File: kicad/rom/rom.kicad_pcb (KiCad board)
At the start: 2 copper layers, 102.5 x 30 mm, 4 parts, among them J1 Board Connector, U1 28C256

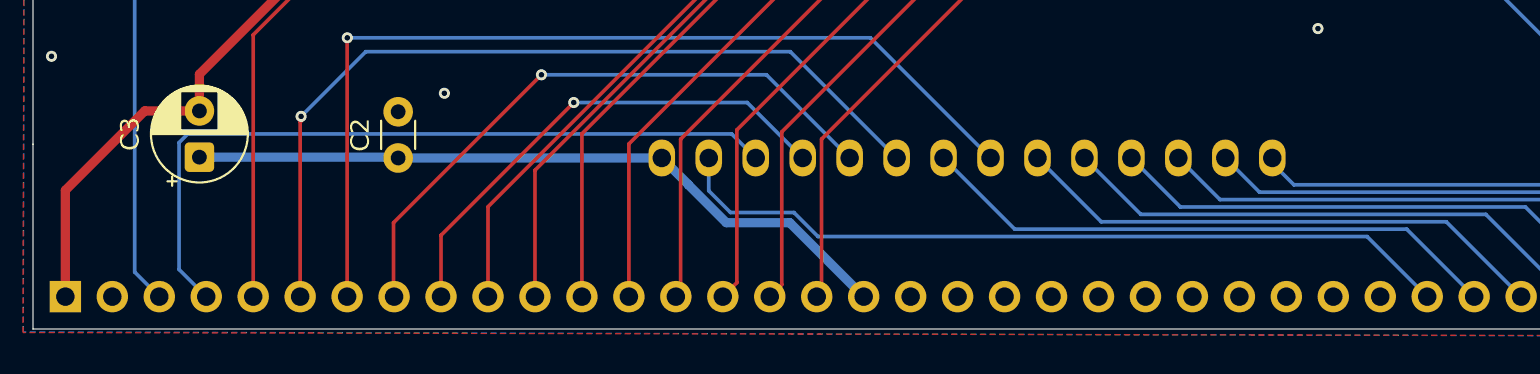
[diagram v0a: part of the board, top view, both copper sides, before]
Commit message: integrated wozmon, updated kicad to specify phi1o
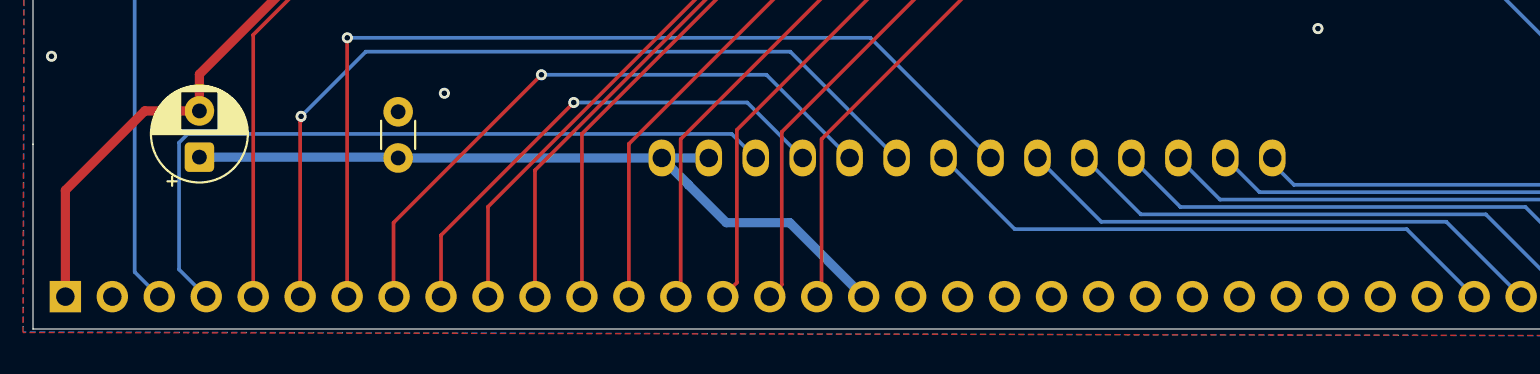
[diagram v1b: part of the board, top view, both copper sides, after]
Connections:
- net PHI2 renamed PHI1
- U1 pad 27: MWRB -> 5V
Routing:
- net MWRB: track 43.0 -> 0.00 mm
- net 5V: track 39.1 -> 41.6 mm
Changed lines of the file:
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@@
 			(at 1.25 -3.75 90)
 			(layer "F.SilkS")
+			(hide yes)
 			(effects
 				(font
@@
 			(at 1.25 3.75 90)
 			(layer "F.Fab")
+			(hide yes)
 			(effects
 				(font
@@
 			(at 1.25 -2.05 90)
 			(layer "F.SilkS")
+			(hide yes)
 			(effects
 				(font
@@
 			(at 1.25 2.05 90)
 			(layer "F.Fab")
+			(hide yes)
 			(effects
 				(font
@@
 			(layers "*.Cu" "*.Mask")
 			(remove_unused_layers no)
-			(net "PHI2")
+			(net "PHI1")
 			(pinfunction "Pin_23_23")
 			(pintype "passive")
@@
 			(at 7.62 11.56 90)
 			(layer "B.SilkS")
+			(hide yes)
 			(effects
 				(font
@@
 			(at 7.62 -40.84 90)
 			(layer "B.Fab")
+			(hide yes)
 			(effects
 				(font
@@
 			(layers "*.Cu" "*.Mask")
 			(remove_unused_layers no)
-			(net "MWRB")
+			(net "5V")
 			(pinfunction "~{WE}_27")
 			(pintype "input")
@@
 	)
 	(segment
+		(start 104.01 120.75)
+		(end 106.55 120.75)
+		(width 0.5)
+		(layer "B.Cu")
+		(net "5V")
+	)
+	(segment
 		(start 89.75 120.75)
 		(end 104.01 120.75)
@@
 	)
 	(segment
-		(start 112.457818 125)
-		(end 142.16 125)
-		(width 0.2)
-		(layer "B.Cu")
-		(net "MWRB")
-	)
-	(segment
-		(start 106.55 122.522182)
-		(end 107.727818 123.7)
-		(width 0.2)
-		(layer "B.Cu")
-		(net "MWRB")
-	)
-	(segment
-		(start 111.157818 123.7)
-		(end 112.457818 125)
-		(width 0.2)
-		(layer "B.Cu")
-		(net "MWRB")
-	)
-	(segment
-		(start 142.16 125)
-		(end 145.41 128.25)
-		(width 0.2)
-		(layer "B.Cu")
-		(net "MWRB")
-	)
-	(segment
-		(start 106.55 120.75)
-		(end 106.55 122.522182)
-		(width 0.2)
-		(layer "B.Cu")
-		(net "MWRB")
-	)
-	(segment
-		(start 107.727818 123.7)
-		(end 111.157818 123.7)
-		(width 0.2)
-		(layer "B.Cu")
-		(net "MWRB")
-	)
-	(segment
